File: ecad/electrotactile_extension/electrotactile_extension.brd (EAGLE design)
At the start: 80 x 38.4 mm, 376 parts, among them IC1 DRV8662, J1 VERT MALE 2.54MM, J2 VERT MALE 2.54MM, J3 VERT MALE 2.54MM, J4 VERT MALE 2.54MM, J5 VERT MALE 2.54MM, J6 PTH VERT MALE, J7 PTH VERT MALE, J8 PTH VERT MALE, J9 PTH VERT MALE, Q1 MCH3474 4A/30V, Q2 MCH3474 4A/30V, Q3 MCH3474 4A/30V, Q4 MCH3474 4A/30V, Q5 MCH3474 4A/30V, Q6 MCH3474 4A/30V, SW1 4A/28V, SW2 25mA/24V

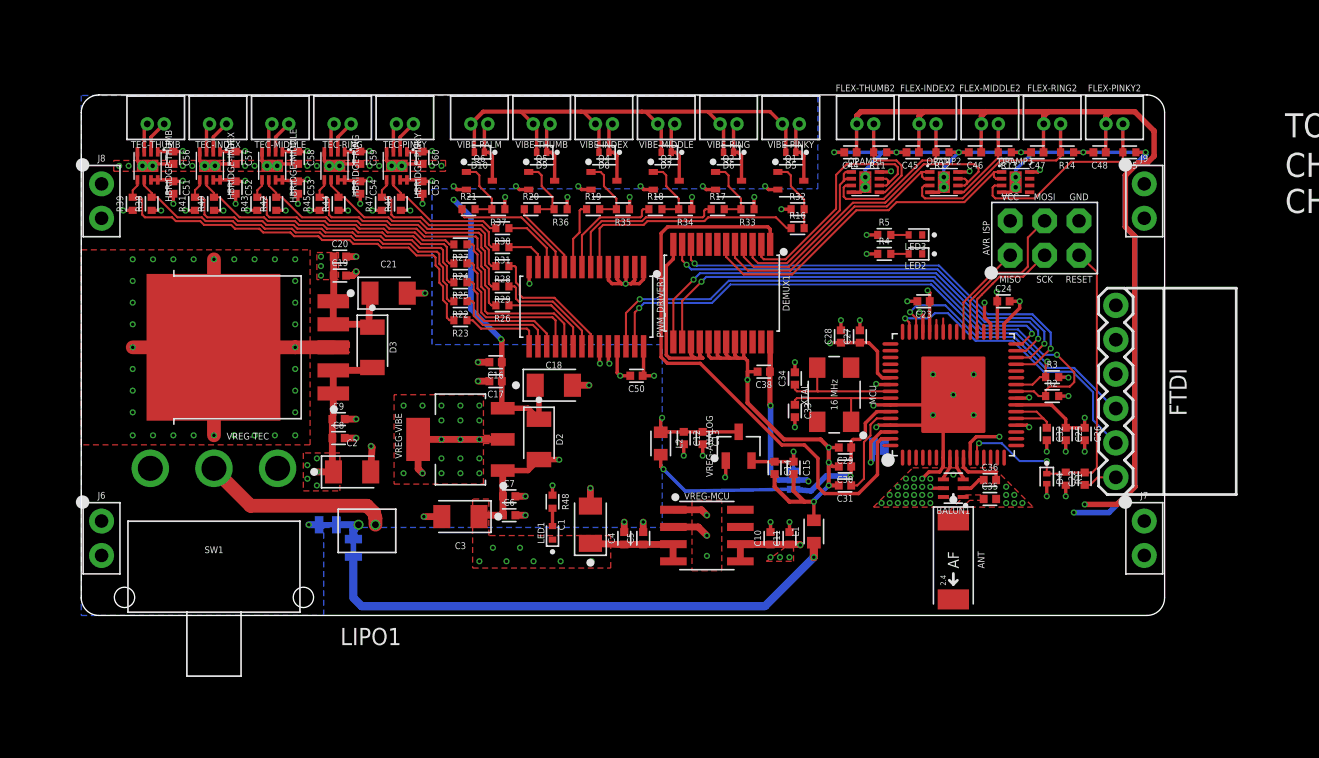
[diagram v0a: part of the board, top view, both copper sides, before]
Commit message: Create Electrotactile Extension board.
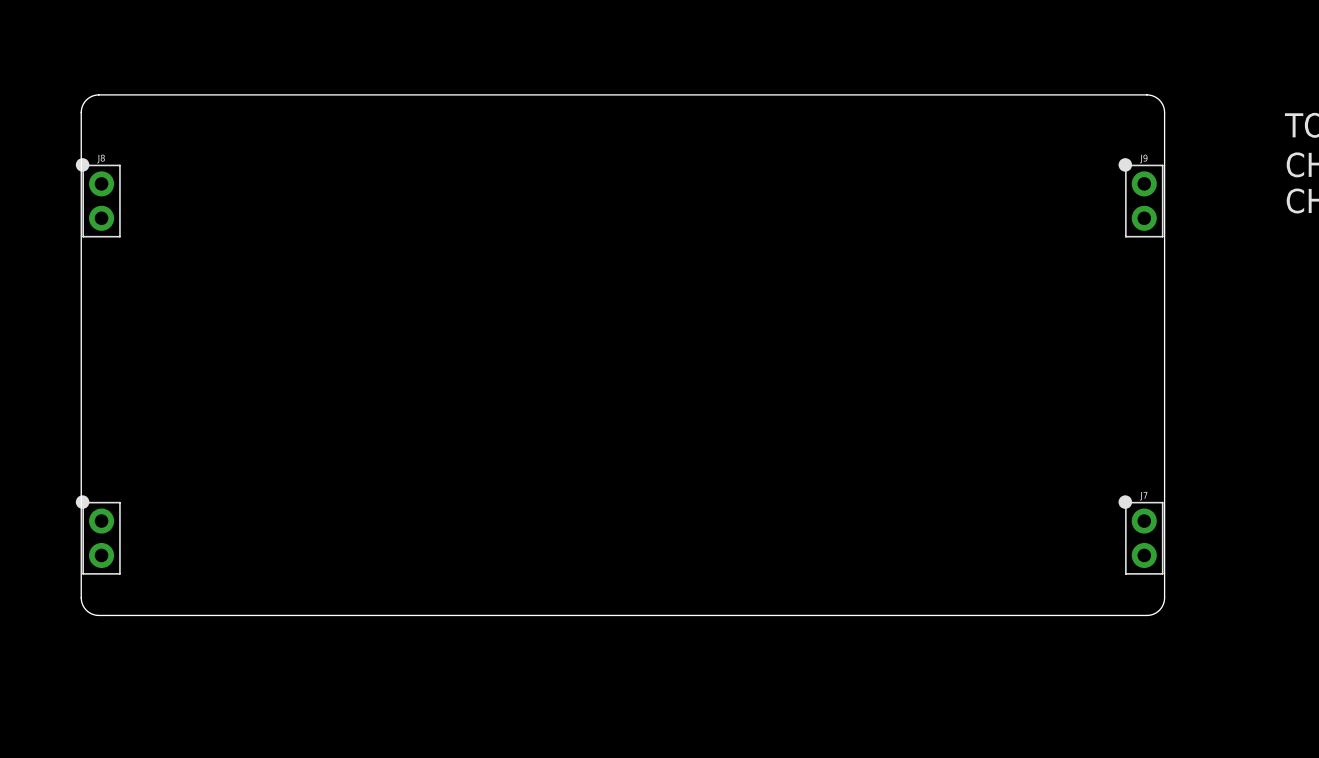
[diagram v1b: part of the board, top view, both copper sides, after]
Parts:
- removed ANT: 2.45GHz, _radio_frequency:ANTC6522X100
- removed AVR_ISP: PTH VERT MALE, _connectors:HDRV6W64P254_2X3_762X483X838B_AVR-ISP
- removed BALUN1: 50/100, _radio_frequency:RESCAXE65P200X125X95-6
- removed BR_ANALOG, BR_NOISE: NET_BRIDGE, _power_symbols:NET_BRIDGE
- removed C1, C18, C2, C21, C3: 100uF/10V, _capacitors:CAPCP3216X160
- removed C10, C13, C14, C16, C19, C22, C23, C25, C27, C30, C38, C44, C45, C46, C47, C48, C5, C50, C51, C52, C53, C54, C55, C56, C57, C58, C59, C60, C7, C9: 0.1uF/50V, _capacitors:CAPC1005X55_SMD-0402
- removed C11, C12, C15, C17, C20, C4, C6, C8: 10uF/6.3V, _capacitors:CAPC1005X55_SMD-0402
- removed C24, C26, C28, C29, C31, C32: 1uF/25V, _capacitors:CAPC1005X55_SMD-0402
- removed C33, C34: 12pF/100V, _capacitors:CAPC1005X55_SMD-0402
- removed C35: 0.75pF/50V, _capacitors:CAPC1005X55_SMD-0402
- removed C36: 22pF/100V, _capacitors:CAPC1005X55_SMD-0402
- removed D10, D4, D5, D6, D7, D8, D9: 150mA/75V, _discrete_semiconductors:DFN100X60X55-2
- removed D2, D3: 1A/50V, _discrete_semiconductors:SODFL3516X170
- removed DEMUX1: CH16_MUX-DEMUX, _special:SOP65P780X200-24
- removed FLEX-INDEX2, FLEX-MIDDLE2, FLEX-PINKY2, FLEX-RING2, FLEX-THUMB2: 10K, _sensors:_MOLEX-0530470210_VERT_PITCH-1.25MM
- removed FTDI: FTDI, _connectors:FTDI_BASIC-6PIN-MALE-RA
- removed HBRIDGE-INDEX, HBRIDGE-MIDDLE, HBRIDGE-PINKY, HBRIDGE-RING, HBRIDGE-THUMB: DRV8837C 1A, _special:WSON-8-PPAD
- removed JP1: JUMPER_SMD_3-PAD_NO_SILK, _connectors:SMT-JUMPER_3_NO_SILK
- removed JP2: JUMPER_SMD_2-PAD_NO_SILK, _connectors:SMT-JUMPER_2_NO_SILK
- removed L1, L2: 10uH/380mA, _inductors:INDC1608X60-0603
- removed LED1: BLUE, _leds:LEDC1005X40_LED-0402
- removed LED2: GREEN, _leds:LEDC1005X40_LED-0402
- removed LED3: RED, _leds:LEDC1005X40_LED-0402
- removed LIPO1: 7.4V, _batteries:BATTERY_MOLEX-0530470210_VERT_PITCH-1.25MM
- removed MCU: ATMEGA128RFA1, _ic_microcontrollers:QFN50P900X900X90-64
- removed OPAMP1, OPAMP2, OPAMP3: LM358, _op_amps:WSON-8-PPAD
- removed PWM_DRIVER1: PCA9685, _special:SOP65P650X110-28
- removed Q1, Q2, Q3, Q4, Q5, Q6: MCH3474 4A/30V, _transistors:SOTFL65P209X90-3
- removed R1, R11, R12, R13, R14, R15, R32, R33, R34, R35, R36, R37, R38, R39, R40, R41, R42, R43, R44, R45, R46, R47, R48: 10K, _resistors:RESC1005X35_SMD-0402
- removed R16, R17, R18, R19, R20, R21, R22, R23, R24, R25, R26, R27, R28, R29, R30, R31: 100, _resistors:RESC1005X35_SMD-0402
- removed R2, R3: 4.7K, _resistors:RESC1005X35_SMD-0402
- removed R4, R5: 1K, _resistors:RESC1005X35_SMD-0402
- removed SW1: 4A/28V, _switches:SW_SLIDE_SPDT_RA_PTH_12.7L-9.5W
- removed TEC-INDEX, TEC-MIDDLE, TEC-PINKY, TEC-RING, TEC-THUMB: PELTIER, _actuators:_MOLEX-0530470210_VERT_PITCH-1.25MM
- removed VIBE-INDEX, VIBE-MIDDLE, VIBE-PALM, VIBE-PINKY, VIBE-RING, VIBE-THUMB: Molex VERT 1.25mm pitch, _actuators:_MOLEX-0530470210_VERT_PITCH-1.25MM
- removed VREG-ANALOG: MCP1700-1802 1.8V/200mA, _ic_power:SOT95P237X112-3_SOT-23-3
- removed VREG-MCU: TPS76833QDR 1A/3.3V, _ic_power:SOIC127P600X265-8
- removed VREG-TEC: 3A/1.8V, _ic_power:TO170P1363X457-6
- removed VREG-VIBE: TL1963A-33 1.5A/3.3V, _ic_power:SOT229P700X180-4
- removed XTAL: 16 MHz, _crystals_oscillators_resonators:OSCCC500X320X110_CRYSTAL
- moved U$2 21.9 mm to (59.9, -8.00)
- moved U$1 20.5 mm to (44.9, -8.00)
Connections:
- removed net +: LIPO1.+, SW1.P
- removed net A1.8V: C14.1, C15.1, JP1.1, VREG-ANALOG.2
- removed net AGND: BALUN1.5, C14.2, C15.2, C29.2, C30.2, C31.2, C35.2, C36.2, C38.2, C44.2, C45.2, C46.2, C47.2, C48.2, DEMUX1.12, DEMUX1.15, DEMUX1.16, DEMUX1.17, DEMUX1.18, DEMUX1.19, DEMUX1.20, DEMUX1.21, DEMUX1.22, DEMUX1.23, DEMUX1.7, DEMUX1.8, DEMUX1.9, L1.2, MCU.10, MCU.58, MCU.61, MCU.7, MCU.EP, MCU.P$1, MCU.P$2, MCU.P$3, MCU.P$4, MCU.P$5, OPAMP1.4, OPAMP1.GND, OPAMP1.P$1, OPAMP1.P$2, OPAMP2.4, OPAMP2.GND, OPAMP2.P$1, OPAMP2.P$2, OPAMP3.4, OPAMP3.GND, OPAMP3.P$1, OPAMP3.P$2, R11.1, R12.1, R13.1, R14.1, R15.1
- removed net AREF: JP2.2, MCU.62
- removed net AVCC: C29.1, C30.1, JP1.3, L2.2, MCU.59
- removed net FLEX-INDEX2: DEMUX1.3, OPAMP1.1, OPAMP1.2
- removed net FLEX-MIDDLE2: DEMUX1.4, OPAMP2.6, OPAMP2.7
- removed net FLEX-PINKY2: DEMUX1.6, OPAMP3.1, OPAMP3.2
- removed net FLEX-RING2: DEMUX1.5, OPAMP2.1, OPAMP2.2
- removed net FLEX-THUMB2: DEMUX1.2, OPAMP1.6, OPAMP1.7
- removed net LED_RX: LED3.A, MCU.42
- removed net LED_TX: LED2.A, MCU.43
- removed net MISO: AVR_ISP.MISO, MCU.39
- removed net MOSI: AVR_ISP.MOSI, MCU.38
- removed net N$1: HBRIDGE-THUMB.3, TEC-THUMB.1
- removed net N$10: HBRIDGE-INDEX.6, R24.2, R40.2
- removed net N$10001: FLEX-PINKY2.2, OPAMP3.3, R15.2
- removed net N$1004: FLEX-THUMB2.2, OPAMP1.5, R11.2
- removed net N$11: HBRIDGE-INDEX.3, TEC-INDEX.1
- removed net N$12: HBRIDGE-MIDDLE.3, TEC-MIDDLE.1
- removed net N$13: HBRIDGE-MIDDLE.5, R27.2, R43.2
- removed net N$14: HBRIDGE-MIDDLE.6, R26.2, R42.2
- removed net N$15: D6.A, Q2.3, VIBE-RING.2
- removed net N$16: HBRIDGE-MIDDLE.2, TEC-MIDDLE.2
- removed net N$17: D5.A, Q1.3, VIBE-PINKY.2
- removed net N$18: HBRIDGE-RING.3, TEC-RING.1
- removed net N$19: HBRIDGE-RING.5, R29.2, R45.2
- removed net N$2: D8.A, Q4.3, VIBE-INDEX.2
- removed net N$20: HBRIDGE-RING.6, R28.2, R44.2
- removed net N$21: Q4.1, R19.2, R35.2
- removed net N$22: Q5.1, R20.2, R36.2
- removed net N$23: HBRIDGE-RING.2, TEC-RING.2
- removed net N$24: HBRIDGE-PINKY.3, TEC-PINKY.1
- removed net N$25: HBRIDGE-PINKY.5, R31.2, R47.2
- removed net N$26: HBRIDGE-PINKY.6, R30.2, R46.2
- removed net N$27: HBRIDGE-PINKY.2, TEC-PINKY.2
- removed net N$28: Q1.1, R16.2, R32.2
- removed net N$29: HBRIDGE-THUMB.5, R23.2, R39.2
- removed net N$3: D9.A, Q5.3, VIBE-THUMB.2
- removed net N$30: D10.A, Q6.3, VIBE-PALM.2
- removed net N$31: HBRIDGE-THUMB.6, R22.2, R38.2
- removed net N$32: Q6.1, R21.2, R37.2
- removed net N$35: C34.1, MCU.56, XTAL.3
- removed net N$36: C33.1, MCU.57, XTAL.1
- removed net N$38: FLEX-INDEX2.2, OPAMP1.3, R12.2
- removed net N$4: D7.A, Q3.3, VIBE-MIDDLE.2
- removed net N$40: BR_ANALOG.P$2, L1.1
- removed net N$41: FLEX-RING2.2, OPAMP2.3, R14.2
- removed net N$45: BALUN1.3, MCU.9
- removed net N$46: BALUN1.4, MCU.8
- removed net N$47: BALUN1.2, C36.1
- removed net N$5: HBRIDGE-THUMB.2, TEC-THUMB.2
- removed net N$50: C22.1, FTDI.DTR
- removed net N$53: LED1.K, R48.2
- removed net N$54: LED2.K, R4.2
- removed net N$55: LED3.K, R5.2
- removed net N$6: HBRIDGE-INDEX.2, TEC-INDEX.2
- removed net N$62: C32.1, MCU.21, MCU.22
- removed net N$63: C31.1, MCU.60
- removed net N$8: HBRIDGE-INDEX.5, R25.2, R41.2
- removed net N$9: Q3.1, R18.2, R34.2
- removed net N$991: FLEX-MIDDLE2.2, OPAMP2.5, R13.2
- removed net RESET: AVR_ISP.RESET, C22.2, D4.A, MCU.12, R1.1
- removed net RFSIG: ANT.1, BALUN1.1, C35.1
- removed net RX0: FTDI.TXO, MCU.46
- removed net S0: DEMUX1.10, MCU.29
- removed net S1: DEMUX1.11, MCU.30
- removed net S2: DEMUX1.14, MCU.32
- removed net S3: DEMUX1.13, MCU.31
- removed net SCK: AVR_ISP.SCK, MCU.37
- removed net SIG: DEMUX1.1, MCU.63
- removed net TEC-INDEX-COLD: PWM_DRIVER1.17, R25.1
- removed net TEC-INDEX-HOT: PWM_DRIVER1.18, R24.1
- removed net TEC-MIDDLE-COLD: PWM_DRIVER1.19, R27.1
- removed net TEC-MIDDLE-HOT: PWM_DRIVER1.20, R26.1
- removed net TEC-PINKY-COLD: PWM_DRIVER1.13, R31.1
- removed net TEC-PINKY-HOT: PWM_DRIVER1.12, R30.1
- removed net TEC-RING-COLD: PWM_DRIVER1.21, R29.1
- removed net TEC-RING-HOT: PWM_DRIVER1.22, R28.1
- removed net TEC-THUMB-COLD: PWM_DRIVER1.15, R23.1
- removed net TEC-THUMB-HOT: PWM_DRIVER1.16, R22.1
- removed net TX0: FTDI.RXI, MCU.47
- removed net VIBE-INDEX: PWM_DRIVER1.9, R19.1
- removed net VIBE-MIDDLE: PWM_DRIVER1.8, R18.1
- removed net VIBE-PALM: PWM_DRIVER1.11, R21.1
- removed net VIBE-PINKY: PWM_DRIVER1.6, R16.1
- removed net VIBE-RING: PWM_DRIVER1.7, R17.1
- removed net VIBE-THUMB: PWM_DRIVER1.10, R20.1
- removed net VSENSOR: C38.1, C44.1, C45.1, C46.1, C47.1, C48.1, DEMUX1.24, FLEX-INDEX2.1, FLEX-MIDDLE2.1, FLEX-PINKY2.1, FLEX-RING2.1, FLEX-THUMB2.1, JP1.2, JP2.1, OPAMP1.8, OPAMP2.8, OPAMP3.8
- net 1.8V: no longer C19.1, C20.1, C21.A, C56.1, C57.1, C58.1, C59.1, C60.1, D3.A, HBRIDGE-INDEX.1, HBRIDGE-MIDDLE.1, HBRIDGE-PINKY.1, HBRIDGE-RING.1, HBRIDGE-THUMB.1, VREG-TEC.4, VREG-TEC.5
- net 3.3V: no longer C16.1, C17.1, C18.A, D10.K, D2.A, D5.K, D6.K, D7.K, D8.K, D9.K, VIBE-INDEX.1, VIBE-MIDDLE.1, VIBE-PALM.1, VIBE-PINKY.1, VIBE-RING.1, VIBE-THUMB.1, VREG-VIBE.3
- net GND: now also J6.2; no longer AVR_ISP.GND, BR_ANALOG.P$1, BR_NOISE.P$2, C10.2, C11.2, C12.2, C13.2, C23.2, C24.2, C25.2, C26.2, C27.2, C28.2, C32.2, C33.2, C34.2, C50.2, C51.2, C52.2, C53.2, C54.2, C55.2, FTDI.GND, LIPO1.-, MCU.11, MCU.20, MCU.24, MCU.33, MCU.35, MCU.45, MCU.55, PWM_DRIVER1.1, PWM_DRIVER1.14, PWM_DRIVER1.2, PWM_DRIVER1.23, PWM_DRIVER1.24, PWM_DRIVER1.25, PWM_DRIVER1.3, PWM_DRIVER1.4, PWM_DRIVER1.5, R32.1, R33.1, R34.1, R35.1, R36.1, R37.1, R38.1, R39.1, R4.1, R40.1, R41.1, R42.1, R43.1, R44.1, R45.1, R46.1, R47.1, R5.1, VREG-ANALOG.1, VREG-MCU.1, VREG-MCU.2
- net N$7: no longer Q2.1, R17.2, R33.2
- net NGND: no longer BR_NOISE.P$1, C1.K, C16.2, C17.2, C18.K, C19.2, C2.K, C20.2, C21.K, C3.K, C4.2, C5.2, C56.2, C57.2, C58.2, C59.2, C6.2, C60.2, C7.2, C8.2, C9.2, HBRIDGE-INDEX.4, HBRIDGE-INDEX.GND, HBRIDGE-INDEX.P$1, HBRIDGE-INDEX.P$2, HBRIDGE-MIDDLE.4, HBRIDGE-MIDDLE.GND, HBRIDGE-MIDDLE.P$1, HBRIDGE-MIDDLE.P$2, HBRIDGE-PINKY.4, HBRIDGE-PINKY.GND, HBRIDGE-PINKY.P$1, HBRIDGE-PINKY.P$2, HBRIDGE-RING.4, HBRIDGE-RING.GND, HBRIDGE-RING.P$1, HBRIDGE-RING.P$2, HBRIDGE-THUMB.4, HBRIDGE-THUMB.GND, HBRIDGE-THUMB.P$1, HBRIDGE-THUMB.P$2, Q1.2, Q2.2, Q3.2, Q4.2, Q5.2, Q6.2, R48.1, VREG-TEC.3, VREG-TEC.TAB, VREG-VIBE.2, VREG-VIBE.TAB
- net SCL: now also J7.2; no longer MCU.25, PWM_DRIVER1.26, R2.1
- net SDA: now also J7.1; no longer MCU.26, PWM_DRIVER1.27, R3.1
- net VBAT: now also J6.1; no longer C1.A, C2.A, C3.A, C4.1, C5.1, C6.1, C7.1, C8.1, C9.1, D2.K, D3.K, LED1.A, SW1.S1, VREG-MCU.3, VREG-MCU.4, VREG-TEC.1, VREG-TEC.2, VREG-VIBE.1
- net VCC: no longer C10.1, C11.1, C12.1, C13.1, C23.1, C24.1, C25.1, C26.1, C27.1, C28.1, C50.1, C51.1, C52.1, C53.1, C54.1, C55.1, D4.K, HBRIDGE-INDEX.7, HBRIDGE-INDEX.8, HBRIDGE-MIDDLE.7, HBRIDGE-MIDDLE.8, HBRIDGE-PINKY.7, HBRIDGE-PINKY.8, HBRIDGE-RING.7, HBRIDGE-RING.8, HBRIDGE-THUMB.7, HBRIDGE-THUMB.8, L2.1, MCU.23, MCU.34, MCU.44, MCU.54, PWM_DRIVER1.28, R1.2, R2.2, R3.2, VREG-ANALOG.3, VREG-MCU.5, VREG-MCU.6
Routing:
- net AGND: track 187.8 -> 0.00 mm, vias 43 -> 0
- net VSENSOR: track 138.6 -> 0.00 mm, vias 7 -> 0
- net NGND: track 75.4 -> 0.00 mm, vias 86 -> 0
- net 3.3V: track 71.4 -> 0.00 mm, vias 2 -> 0
- net GND: track 65.9 -> 0.00 mm, vias 51 -> 0
- net VCC: track 50.3 -> 0.00 mm, vias 19 -> 0
- net SCL: track 45.2 -> 0.00 mm, vias 2 -> 0
- net SIG: track 44.0 -> 0.00 mm
- net N$40: track 39.9 -> 0.00 mm, vias 1 -> 0
- net SDA: track 39.8 -> 0.00 mm, vias 2 -> 0
- net S3: track 35.2 -> 0.00 mm, vias 2 -> 0
- net S0: track 34.1 -> 0.00 mm, vias 2 -> 0
- net S1: track 33.5 -> 0.00 mm, vias 2 -> 0
- net S2: track 32.9 -> 0.00 mm, vias 2 -> 0
- net N$29: track 31.7 -> 0.00 mm
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- removed copper zone on layer 1, net 1.8V
- removed copper zone on layer 2, net 1.8V
- removed copper zone on layer 1, net AGND
- removed copper zone on layer 15, net AGND
- removed copper zone on layer 1, net GND
- removed copper zone on layer 15, net N$34
- removed copper zone on layer 2, net N$34
- removed copper zone on layer 2, net N$37
- removed copper zone on layer 1, net NGND
- removed copper zone on layer 15, net NGND
- removed copper zone on layer 16, net NGND
- removed copper zone on layer 1, net RFSIG
- removed copper zone on layer 1, net VBAT
- removed copper zone on layer 2, net VBAT
- removed copper zone on layer 1, net VCC
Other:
- board text removed: "Designed by: &"

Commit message: Update work on Electrotactile extension board.  Add doc folder with several schematics breaking down the transmission of touch for documentation purposes.
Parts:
- removed ET_INDEX_PIXEL1-10, ET_INDEX_PIXEL1-11, ET_INDEX_PIXEL1-12, ET_INDEX_PIXEL1-13, ET_INDEX_PIXEL1-14, ET_INDEX_PIXEL1-15, ET_INDEX_PIXEL1-16, ET_INDEX_PIXEL1-17, ET_INDEX_PIXEL1-18, ET_INDEX_PIXEL1-19, ET_INDEX_PIXEL1-20, ET_INDEX_PIXEL1-5, ET_INDEX_PIXEL1-6, ET_INDEX_PIXEL1-7, ET_INDEX_PIXEL1-8, ET_INDEX_PIXEL1-9, ET_INDEX_PIXEL2-10, ET_INDEX_PIXEL2-11, ET_INDEX_PIXEL2-12, ET_INDEX_PIXEL2-13, ET_INDEX_PIXEL2-14, ET_INDEX_PIXEL2-15, ET_INDEX_PIXEL2-16, ET_INDEX_PIXEL2-17, ET_INDEX_PIXEL2-18, ET_INDEX_PIXEL2-19, ET_INDEX_PIXEL2-20, ET_INDEX_PIXEL2-5, ET_INDEX_PIXEL2-6, ET_INDEX_PIXEL2-7, ET_INDEX_PIXEL2-8, ET_INDEX_PIXEL2-9, ET_INDEX_PIXEL3-10, ET_INDEX_PIXEL3-11, ET_INDEX_PIXEL3-12, ET_INDEX_PIXEL3-13, ET_INDEX_PIXEL3-14, ET_INDEX_PIXEL3-15, ET_INDEX_PIXEL3-16, ET_INDEX_PIXEL3-17, ET_INDEX_PIXEL3-18, ET_INDEX_PIXEL3-19, ET_INDEX_PIXEL3-20, ET_INDEX_PIXEL3-5, ET_INDEX_PIXEL3-6, ET_INDEX_PIXEL3-7, ET_INDEX_PIXEL3-8, ET_INDEX_PIXEL3-9, ET_INDEX_PIXEL4-10, ET_INDEX_PIXEL4-11, ET_INDEX_PIXEL4-12, ET_INDEX_PIXEL4-13, ET_INDEX_PIXEL4-14, ET_INDEX_PIXEL4-15, ET_INDEX_PIXEL4-16, ET_INDEX_PIXEL4-17, ET_INDEX_PIXEL4-18, ET_INDEX_PIXEL4-19, ET_INDEX_PIXEL4-20, ET_INDEX_PIXEL4-5, ET_INDEX_PIXEL4-6, ET_INDEX_PIXEL4-7, ET_INDEX_PIXEL4-8, ET_INDEX_PIXEL4-9: SPST-NO 170mA 250V, _relay:SOP254P609X203-4
- removed PWM_DRIVER2, PWM_DRIVER3, PWM_DRIVER4, PWM_DRIVER5, PWM_DRIVER6: PCA9685, _special:SOP65P650X110-28
- added ET_MIDDLE_PIXEL1-1, ET_MIDDLE_PIXEL1-2, ET_MIDDLE_PIXEL1-3, ET_MIDDLE_PIXEL1-4, ET_MIDDLE_PIXEL2-1, ET_MIDDLE_PIXEL2-2, ET_MIDDLE_PIXEL2-3, ET_MIDDLE_PIXEL2-4, ET_MIDDLE_PIXEL3-1, ET_MIDDLE_PIXEL3-2, ET_MIDDLE_PIXEL3-3, ET_MIDDLE_PIXEL3-4, ET_MIDDLE_PIXEL4-1, ET_MIDDLE_PIXEL4-2, ET_MIDDLE_PIXEL4-3, ET_MIDDLE_PIXEL4-4, ET_PINKY_PIXEL1-1, ET_PINKY_PIXEL1-2, ET_PINKY_PIXEL1-3, ET_PINKY_PIXEL1-4, ET_PINKY_PIXEL2-1, ET_PINKY_PIXEL2-2, ET_PINKY_PIXEL2-3, ET_PINKY_PIXEL2-4, ET_PINKY_PIXEL3-1, ET_PINKY_PIXEL3-2, ET_PINKY_PIXEL3-3, ET_PINKY_PIXEL3-4, ET_PINKY_PIXEL4-1, ET_PINKY_PIXEL4-2, ET_PINKY_PIXEL4-3, ET_PINKY_PIXEL4-4, ET_RING_PIXEL1-1, ET_RING_PIXEL1-2, ET_RING_PIXEL1-3, ET_RING_PIXEL1-4, ET_RING_PIXEL2-1, ET_RING_PIXEL2-2, ET_RING_PIXEL2-3, ET_RING_PIXEL2-4, ET_RING_PIXEL3-1, ET_RING_PIXEL3-2, ET_RING_PIXEL3-3, ET_RING_PIXEL3-4, ET_RING_PIXEL4-1, ET_RING_PIXEL4-2, ET_RING_PIXEL4-3, ET_RING_PIXEL4-4, ET_THUMB_PIXEL1-1, ET_THUMB_PIXEL1-2, ET_THUMB_PIXEL1-3, ET_THUMB_PIXEL1-4, ET_THUMB_PIXEL2-1, ET_THUMB_PIXEL2-2, ET_THUMB_PIXEL2-3, ET_THUMB_PIXEL2-4, ET_THUMB_PIXEL3-1, ET_THUMB_PIXEL3-2, ET_THUMB_PIXEL3-3, ET_THUMB_PIXEL3-4, ET_THUMB_PIXEL4-1, ET_THUMB_PIXEL4-2, ET_THUMB_PIXEL4-3, ET_THUMB_PIXEL4-4: SPST-NO 170mA 250V, _relay:SOP254P609X203-4
- added MUX_INDEX, MUX_MIDDLE, MUX_PINKY, MUX_RING, MUX_THUMB: PCA9685, _special:SOP65P650X110-28
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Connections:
- new net MIDDLE_IN1-1: ET_MIDDLE_PIXEL1-1.1, MUX_MIDDLE.21
- new net MIDDLE_IN1-2: ET_MIDDLE_PIXEL1-2.1, MUX_MIDDLE.19
- new net MIDDLE_IN1-3: ET_MIDDLE_PIXEL1-3.1, MUX_MIDDLE.17
- new net MIDDLE_IN1-4: ET_MIDDLE_PIXEL1-4.1, MUX_MIDDLE.15
- new net MIDDLE_IN2-1: ET_MIDDLE_PIXEL2-1.1, MUX_MIDDLE.22
- new net MIDDLE_IN2-2: ET_MIDDLE_PIXEL2-2.1, MUX_MIDDLE.20
- new net MIDDLE_IN2-3: ET_MIDDLE_PIXEL2-3.1, MUX_MIDDLE.18
- new net MIDDLE_IN2-4: ET_MIDDLE_PIXEL2-4.1, MUX_MIDDLE.16
- new net MIDDLE_IN3-1: ET_MIDDLE_PIXEL3-1.1, MUX_MIDDLE.12
- new net MIDDLE_IN3-2: ET_MIDDLE_PIXEL3-2.1, MUX_MIDDLE.10
- new net MIDDLE_IN3-3: ET_MIDDLE_PIXEL3-3.1, MUX_MIDDLE.8
- new net MIDDLE_IN3-4: ET_MIDDLE_PIXEL3-4.1, MUX_MIDDLE.6
- new net MIDDLE_IN4-1: ET_MIDDLE_PIXEL4-1.1, MUX_MIDDLE.13
- new net MIDDLE_IN4-2: ET_MIDDLE_PIXEL4-2.1, MUX_MIDDLE.11
- new net MIDDLE_IN4-3: ET_MIDDLE_PIXEL4-3.1, MUX_MIDDLE.9
- new net MIDDLE_IN4-4: ET_MIDDLE_PIXEL4-4.1, MUX_MIDDLE.7
- new net MIDDLE_OUT1-1: ET_MIDDLE_PIXEL1-1.3
- new net MIDDLE_OUT1-2: ET_MIDDLE_PIXEL1-2.3
- new net MIDDLE_OUT1-3: ET_MIDDLE_PIXEL1-3.3
- new net MIDDLE_OUT1-4: ET_MIDDLE_PIXEL1-4.3
- new net MIDDLE_OUT2-1: ET_MIDDLE_PIXEL2-1.3
- new net MIDDLE_OUT2-2: ET_MIDDLE_PIXEL2-2.3
- new net MIDDLE_OUT2-3: ET_MIDDLE_PIXEL2-3.3
- new net MIDDLE_OUT2-4: ET_MIDDLE_PIXEL2-4.3
- new net MIDDLE_OUT3-1: ET_MIDDLE_PIXEL3-1.3
- new net MIDDLE_OUT3-2: ET_MIDDLE_PIXEL3-2.3
- new net MIDDLE_OUT3-3: ET_MIDDLE_PIXEL3-3.3
- new net MIDDLE_OUT3-4: ET_MIDDLE_PIXEL3-4.3
- new net MIDDLE_OUT4-1: ET_MIDDLE_PIXEL4-1.3
- new net MIDDLE_OUT4-2: ET_MIDDLE_PIXEL4-2.3
- new net MIDDLE_OUT4-3: ET_MIDDLE_PIXEL4-3.3
- new net MIDDLE_OUT4-4: ET_MIDDLE_PIXEL4-4.3
- new net PINKY_IN1-1: ET_PINKY_PIXEL1-1.1, MUX_PINKY.22
- new net PINKY_IN1-2: ET_PINKY_PIXEL1-2.1, MUX_PINKY.20
- new net PINKY_IN1-3: ET_PINKY_PIXEL1-3.1, MUX_PINKY.18
- new net PINKY_IN1-4: ET_PINKY_PIXEL1-4.1, MUX_PINKY.16
- new net PINKY_IN2-1: ET_PINKY_PIXEL2-1.1, MUX_PINKY.21
- new net PINKY_IN2-2: ET_PINKY_PIXEL2-2.1, MUX_PINKY.19
- new net PINKY_IN2-3: ET_PINKY_PIXEL2-3.1, MUX_PINKY.17
- new net PINKY_IN2-4: ET_PINKY_PIXEL2-4.1, MUX_PINKY.15
- new net PINKY_IN3-1: ET_PINKY_PIXEL3-1.1, MUX_PINKY.13
- new net PINKY_IN3-2: ET_PINKY_PIXEL3-2.1, MUX_PINKY.11
- new net PINKY_IN3-3: ET_PINKY_PIXEL3-3.1, MUX_PINKY.9
- new net PINKY_IN3-4: ET_PINKY_PIXEL3-4.1, MUX_PINKY.7
- new net PINKY_IN4-1: ET_PINKY_PIXEL4-1.1, MUX_PINKY.12
- new net PINKY_IN4-2: ET_PINKY_PIXEL4-2.1, MUX_PINKY.10
- new net PINKY_IN4-3: ET_PINKY_PIXEL4-3.1, MUX_PINKY.8
- new net PINKY_IN4-4: ET_PINKY_PIXEL4-4.1, MUX_PINKY.6
- new net PINKY_OUT1-1: ET_PINKY_PIXEL1-1.3
- new net PINKY_OUT1-2: ET_PINKY_PIXEL1-2.3
- new net PINKY_OUT1-3: ET_PINKY_PIXEL1-3.3
- new net PINKY_OUT1-4: ET_PINKY_PIXEL1-4.3
- new net PINKY_OUT2-1: ET_PINKY_PIXEL2-1.3
- new net PINKY_OUT2-2: ET_PINKY_PIXEL2-2.3
- new net PINKY_OUT2-3: ET_PINKY_PIXEL2-3.3
- new net PINKY_OUT2-4: ET_PINKY_PIXEL2-4.3
- new net PINKY_OUT3-1: ET_PINKY_PIXEL3-1.3
- new net PINKY_OUT3-2: ET_PINKY_PIXEL3-2.3
- new net PINKY_OUT3-3: ET_PINKY_PIXEL3-3.3
- new net PINKY_OUT3-4: ET_PINKY_PIXEL3-4.3
- new net PINKY_OUT4-1: ET_PINKY_PIXEL4-1.3
- new net PINKY_OUT4-2: ET_PINKY_PIXEL4-2.3
- new net PINKY_OUT4-3: ET_PINKY_PIXEL4-3.3
- new net PINKY_OUT4-4: ET_PINKY_PIXEL4-4.3
- new net RING_IN1-1: ET_RING_PIXEL1-1.1, MUX_RING.7
- new net RING_IN1-2: ET_RING_PIXEL1-2.1, MUX_RING.9
- new net RING_IN1-3: ET_RING_PIXEL1-3.1, MUX_RING.11
- new net RING_IN1-4: ET_RING_PIXEL1-4.1, MUX_RING.13
- new net RING_IN2-1: ET_RING_PIXEL2-1.1, MUX_RING.6
- new net RING_IN2-2: ET_RING_PIXEL2-2.1, MUX_RING.8
- new net RING_IN2-3: ET_RING_PIXEL2-3.1, MUX_RING.10
- new net RING_IN2-4: ET_RING_PIXEL2-4.1, MUX_RING.12
- new net RING_IN3-1: ET_RING_PIXEL3-1.1, MUX_RING.16
- new net RING_IN3-2: ET_RING_PIXEL3-2.1, MUX_RING.18
- new net RING_IN3-3: ET_RING_PIXEL3-3.1, MUX_RING.20
- new net RING_IN3-4: ET_RING_PIXEL3-4.1, MUX_RING.22
- new net RING_IN4-1: ET_RING_PIXEL4-1.1, MUX_RING.15
- new net RING_IN4-2: ET_RING_PIXEL4-2.1, MUX_RING.17
- new net RING_IN4-3: ET_RING_PIXEL4-3.1, MUX_RING.19
- new net RING_IN4-4: ET_RING_PIXEL4-4.1, MUX_RING.21
- new net RING_OUT1-1: ET_RING_PIXEL1-1.3
- new net RING_OUT1-2: ET_RING_PIXEL1-2.3
- new net RING_OUT1-3: ET_RING_PIXEL1-3.3
- new net RING_OUT1-4: ET_RING_PIXEL1-4.3
- new net RING_OUT2-1: ET_RING_PIXEL2-1.3
- new net RING_OUT2-2: ET_RING_PIXEL2-2.3
- new net RING_OUT2-3: ET_RING_PIXEL2-3.3
- new net RING_OUT2-4: ET_RING_PIXEL2-4.3
- new net RING_OUT3-1: ET_RING_PIXEL3-1.3
- new net RING_OUT3-2: ET_RING_PIXEL3-2.3
- new net RING_OUT3-3: ET_RING_PIXEL3-3.3
- new net RING_OUT3-4: ET_RING_PIXEL3-4.3
- new net RING_OUT4-1: ET_RING_PIXEL4-1.3
- new net RING_OUT4-2: ET_RING_PIXEL4-2.3
- new net RING_OUT4-3: ET_RING_PIXEL4-3.3
- new net RING_OUT4-4: ET_RING_PIXEL4-4.3
- new net THUMB_IN1-1: ET_THUMB_PIXEL1-1.1, MUX_THUMB.6
- new net THUMB_IN1-2: ET_THUMB_PIXEL1-2.1, MUX_THUMB.7
- new net THUMB_IN1-3: ET_THUMB_PIXEL1-3.1, MUX_THUMB.8
- new net THUMB_IN1-4: ET_THUMB_PIXEL1-4.1, MUX_THUMB.9
- new net THUMB_IN2-1: ET_THUMB_PIXEL2-1.1, MUX_THUMB.10
- new net THUMB_IN2-2: ET_THUMB_PIXEL2-2.1, MUX_THUMB.11
- new net THUMB_IN2-3: ET_THUMB_PIXEL2-3.1, MUX_THUMB.12
- new net THUMB_IN2-4: ET_THUMB_PIXEL2-4.1, MUX_THUMB.13
- new net THUMB_IN3-1: ET_THUMB_PIXEL3-1.1, MUX_THUMB.15
- new net THUMB_IN3-2: ET_THUMB_PIXEL3-2.1, MUX_THUMB.16
- new net THUMB_IN3-3: ET_THUMB_PIXEL3-3.1, MUX_THUMB.17
- new net THUMB_IN3-4: ET_THUMB_PIXEL3-4.1, MUX_THUMB.18
- new net THUMB_IN4-1: ET_THUMB_PIXEL4-1.1, MUX_THUMB.19
- new net THUMB_IN4-2: ET_THUMB_PIXEL4-2.1, MUX_THUMB.20
- new net THUMB_IN4-3: ET_THUMB_PIXEL4-3.1, MUX_THUMB.21
- new net THUMB_IN4-4: ET_THUMB_PIXEL4-4.1, MUX_THUMB.22
- new net THUMB_OUT1-1: ET_THUMB_PIXEL1-1.3
- new net THUMB_OUT1-2: ET_THUMB_PIXEL1-2.3
- new net THUMB_OUT1-3: ET_THUMB_PIXEL1-3.3
- new net THUMB_OUT1-4: ET_THUMB_PIXEL1-4.3
- new net THUMB_OUT2-1: ET_THUMB_PIXEL2-1.3
- new net THUMB_OUT2-2: ET_THUMB_PIXEL2-2.3
- new net THUMB_OUT2-3: ET_THUMB_PIXEL2-3.3
- new net THUMB_OUT2-4: ET_THUMB_PIXEL2-4.3
- new net THUMB_OUT3-1: ET_THUMB_PIXEL3-1.3
- new net THUMB_OUT3-2: ET_THUMB_PIXEL3-2.3
- new net THUMB_OUT3-3: ET_THUMB_PIXEL3-3.3
- new net THUMB_OUT3-4: ET_THUMB_PIXEL3-4.3
- new net THUMB_OUT4-1: ET_THUMB_PIXEL4-1.3
- new net THUMB_OUT4-2: ET_THUMB_PIXEL4-2.3
- new net THUMB_OUT4-3: ET_THUMB_PIXEL4-3.3
- new net THUMB_OUT4-4: ET_THUMB_PIXEL4-4.3
- net GND: now also MUX_INDEX.1, MUX_INDEX.14, MUX_INDEX.2, MUX_INDEX.23, MUX_INDEX.24, MUX_INDEX.25, MUX_INDEX.3, MUX_INDEX.4, MUX_INDEX.5, MUX_MIDDLE.1, MUX_MIDDLE.14, MUX_MIDDLE.2, MUX_MIDDLE.23, MUX_MIDDLE.24, MUX_MIDDLE.25, MUX_MIDDLE.3, MUX_MIDDLE.4, MUX_MIDDLE.5, MUX_PINKY.1, MUX_PINKY.14, MUX_PINKY.2, MUX_PINKY.23, MUX_PINKY.24, MUX_PINKY.25, MUX_PINKY.3, MUX_PINKY.4, MUX_PINKY.5, MUX_RING.1, MUX_RING.14, MUX_RING.2, MUX_RING.23, MUX_RING.24, MUX_RING.25, MUX_RING.3, MUX_RING.4, MUX_RING.5, MUX_THUMB.1, MUX_THUMB.14, MUX_THUMB.2, MUX_THUMB.23, MUX_THUMB.24, MUX_THUMB.25, MUX_THUMB.3, MUX_THUMB.4, MUX_THUMB.5; no longer PWM_DRIVER2.1, PWM_DRIVER2.14, PWM_DRIVER2.2, PWM_DRIVER2.23, PWM_DRIVER2.24, PWM_DRIVER2.25, PWM_DRIVER2.3, PWM_DRIVER2.4, PWM_DRIVER2.5, PWM_DRIVER3.1, PWM_DRIVER3.14, PWM_DRIVER3.2, PWM_DRIVER3.23, PWM_DRIVER3.24, PWM_DRIVER3.25, PWM_DRIVER3.3, PWM_DRIVER3.4, PWM_DRIVER3.5, PWM_DRIVER4.1, PWM_DRIVER4.14, PWM_DRIVER4.2, PWM_DRIVER4.23, PWM_DRIVER4.24, PWM_DRIVER4.25, PWM_DRIVER4.3, PWM_DRIVER4.4, PWM_DRIVER4.5, PWM_DRIVER5.1, PWM_DRIVER5.14, PWM_DRIVER5.2, PWM_DRIVER5.23, PWM_DRIVER5.24, PWM_DRIVER5.25, PWM_DRIVER5.3, PWM_DRIVER5.4, PWM_DRIVER5.5, PWM_DRIVER6.1, PWM_DRIVER6.14, PWM_DRIVER6.2, PWM_DRIVER6.23, PWM_DRIVER6.24, PWM_DRIVER6.25, PWM_DRIVER6.3, PWM_DRIVER6.4, PWM_DRIVER6.5
- net INDEX_IN1-1: now also MUX_INDEX.6; no longer ET_INDEX_PIXEL1-13.1, ET_INDEX_PIXEL1-17.1, ET_INDEX_PIXEL1-5.1, ET_INDEX_PIXEL1-9.1, PWM_DRIVER2.6, PWM_DRIVER3.6, PWM_DRIVER4.6, PWM_DRIVER5.6, PWM_DRIVER6.6
- net INDEX_IN1-2: now also MUX_INDEX.8; no longer ET_INDEX_PIXEL1-10.1, ET_INDEX_PIXEL1-14.1, ET_INDEX_PIXEL1-18.1, ET_INDEX_PIXEL1-6.1, PWM_DRIVER2.7, PWM_DRIVER3.7, PWM_DRIVER4.7, PWM_DRIVER5.7, PWM_DRIVER6.7
- net INDEX_IN1-3: now also MUX_INDEX.10; no longer ET_INDEX_PIXEL1-11.1, ET_INDEX_PIXEL1-15.1, ET_INDEX_PIXEL1-19.1, ET_INDEX_PIXEL1-7.1, PWM_DRIVER2.8, PWM_DRIVER3.8, PWM_DRIVER4.8, PWM_DRIVER5.8, PWM_DRIVER6.8
- net INDEX_IN1-4: now also MUX_INDEX.12; no longer ET_INDEX_PIXEL1-12.1, ET_INDEX_PIXEL1-16.1, ET_INDEX_PIXEL1-20.1, ET_INDEX_PIXEL1-8.1, PWM_DRIVER2.9, PWM_DRIVER3.9, PWM_DRIVER4.9, PWM_DRIVER5.9, PWM_DRIVER6.9
- net INDEX_IN2-1: now also MUX_INDEX.7; no longer ET_INDEX_PIXEL2-11.1, ET_INDEX_PIXEL2-15.1, ET_INDEX_PIXEL2-19.1, ET_INDEX_PIXEL2-7.1, PWM_DRIVER2.10, PWM_DRIVER3.10, PWM_DRIVER4.10, PWM_DRIVER5.10, PWM_DRIVER6.10
- net INDEX_IN2-2: now also MUX_INDEX.9; no longer ET_INDEX_PIXEL2-10.1, ET_INDEX_PIXEL2-14.1, ET_INDEX_PIXEL2-18.1, ET_INDEX_PIXEL2-6.1, PWM_DRIVER2.11, PWM_DRIVER3.11, PWM_DRIVER4.11, PWM_DRIVER5.11, PWM_DRIVER6.11
- net INDEX_IN2-3: now also MUX_INDEX.11; no longer ET_INDEX_PIXEL2-13.1, ET_INDEX_PIXEL2-17.1, ET_INDEX_PIXEL2-5.1, ET_INDEX_PIXEL2-9.1, PWM_DRIVER2.12, PWM_DRIVER3.12, PWM_DRIVER4.12, PWM_DRIVER5.12, PWM_DRIVER6.12
- net INDEX_IN2-4: now also MUX_INDEX.13; no longer ET_INDEX_PIXEL2-12.1, ET_INDEX_PIXEL2-16.1, ET_INDEX_PIXEL2-20.1, ET_INDEX_PIXEL2-8.1, PWM_DRIVER2.13, PWM_DRIVER3.13, PWM_DRIVER4.13, PWM_DRIVER5.13, PWM_DRIVER6.13
- net INDEX_IN3-1: now also MUX_INDEX.15; no longer ET_INDEX_PIXEL3-13.1, ET_INDEX_PIXEL3-17.1, ET_INDEX_PIXEL3-5.1, ET_INDEX_PIXEL3-9.1, PWM_DRIVER2.15, PWM_DRIVER3.15, PWM_DRIVER4.15, PWM_DRIVER5.15, PWM_DRIVER6.15
- net INDEX_IN3-2: now also MUX_INDEX.17; no longer ET_INDEX_PIXEL3-10.1, ET_INDEX_PIXEL3-14.1, ET_INDEX_PIXEL3-18.1, ET_INDEX_PIXEL3-6.1, PWM_DRIVER2.16, PWM_DRIVER3.16, PWM_DRIVER4.16, PWM_DRIVER5.16, PWM_DRIVER6.16
- net INDEX_IN3-3: now also MUX_INDEX.19; no longer ET_INDEX_PIXEL3-11.1, ET_INDEX_PIXEL3-15.1, ET_INDEX_PIXEL3-19.1, ET_INDEX_PIXEL3-7.1, PWM_DRIVER2.17, PWM_DRIVER3.17, PWM_DRIVER4.17, PWM_DRIVER5.17, PWM_DRIVER6.17
- net INDEX_IN3-4: now also MUX_INDEX.21; no longer ET_INDEX_PIXEL3-12.1, ET_INDEX_PIXEL3-16.1, ET_INDEX_PIXEL3-20.1, ET_INDEX_PIXEL3-8.1, PWM_DRIVER2.18, PWM_DRIVER3.18, PWM_DRIVER4.18, PWM_DRIVER5.18, PWM_DRIVER6.18
- net INDEX_IN4-1: now also MUX_INDEX.16; no longer ET_INDEX_PIXEL4-13.1, ET_INDEX_PIXEL4-17.1, ET_INDEX_PIXEL4-5.1, ET_INDEX_PIXEL4-9.1, PWM_DRIVER2.19, PWM_DRIVER3.19, PWM_DRIVER4.19, PWM_DRIVER5.19, PWM_DRIVER6.19
- net INDEX_IN4-2: now also MUX_INDEX.18; no longer ET_INDEX_PIXEL4-10.1, ET_INDEX_PIXEL4-14.1, ET_INDEX_PIXEL4-18.1, ET_INDEX_PIXEL4-6.1, PWM_DRIVER2.20, PWM_DRIVER3.20, PWM_DRIVER4.20, PWM_DRIVER5.20, PWM_DRIVER6.20
- net INDEX_IN4-3: now also MUX_INDEX.20; no longer ET_INDEX_PIXEL4-11.1, ET_INDEX_PIXEL4-15.1, ET_INDEX_PIXEL4-19.1, ET_INDEX_PIXEL4-7.1, PWM_DRIVER2.21, PWM_DRIVER3.21, PWM_DRIVER4.21, PWM_DRIVER5.21, PWM_DRIVER6.21
- net INDEX_IN4-4: now also MUX_INDEX.22; no longer ET_INDEX_PIXEL4-12.1, ET_INDEX_PIXEL4-16.1, ET_INDEX_PIXEL4-20.1, ET_INDEX_PIXEL4-8.1, PWM_DRIVER2.22, PWM_DRIVER3.22, PWM_DRIVER4.22, PWM_DRIVER5.22, PWM_DRIVER6.22
- net INDEX_OUT1-1: no longer ET_INDEX_PIXEL1-13.3, ET_INDEX_PIXEL1-17.3, ET_INDEX_PIXEL1-5.3, ET_INDEX_PIXEL1-9.3
- net INDEX_OUT1-2: no longer ET_INDEX_PIXEL1-10.3, ET_INDEX_PIXEL1-14.3, ET_INDEX_PIXEL1-18.3, ET_INDEX_PIXEL1-6.3
- net INDEX_OUT1-3: no longer ET_INDEX_PIXEL1-11.3, ET_INDEX_PIXEL1-15.3, ET_INDEX_PIXEL1-19.3, ET_INDEX_PIXEL1-7.3
- net INDEX_OUT1-4: no longer ET_INDEX_PIXEL1-12.3, ET_INDEX_PIXEL1-16.3, ET_INDEX_PIXEL1-20.3, ET_INDEX_PIXEL1-8.3
- net INDEX_OUT2-1: no longer ET_INDEX_PIXEL2-11.3, ET_INDEX_PIXEL2-15.3, ET_INDEX_PIXEL2-19.3, ET_INDEX_PIXEL2-7.3
- net INDEX_OUT2-2: no longer ET_INDEX_PIXEL2-10.3, ET_INDEX_PIXEL2-14.3, ET_INDEX_PIXEL2-18.3, ET_INDEX_PIXEL2-6.3
- net INDEX_OUT2-3: no longer ET_INDEX_PIXEL2-13.3, ET_INDEX_PIXEL2-17.3, ET_INDEX_PIXEL2-5.3, ET_INDEX_PIXEL2-9.3
- net INDEX_OUT2-4: no longer ET_INDEX_PIXEL2-12.3, ET_INDEX_PIXEL2-16.3, ET_INDEX_PIXEL2-20.3, ET_INDEX_PIXEL2-8.3
- net INDEX_OUT3-1: no longer ET_INDEX_PIXEL3-13.3, ET_INDEX_PIXEL3-17.3, ET_INDEX_PIXEL3-5.3, ET_INDEX_PIXEL3-9.3
- net INDEX_OUT3-2: no longer ET_INDEX_PIXEL3-10.3, ET_INDEX_PIXEL3-14.3, ET_INDEX_PIXEL3-18.3, ET_INDEX_PIXEL3-6.3
- net INDEX_OUT3-3: no longer ET_INDEX_PIXEL3-11.3, ET_INDEX_PIXEL3-15.3, ET_INDEX_PIXEL3-19.3, ET_INDEX_PIXEL3-7.3
- net INDEX_OUT3-4: no longer ET_INDEX_PIXEL3-12.3, ET_INDEX_PIXEL3-16.3, ET_INDEX_PIXEL3-20.3, ET_INDEX_PIXEL3-8.3
- net INDEX_OUT4-1: no longer ET_INDEX_PIXEL4-13.3, ET_INDEX_PIXEL4-17.3, ET_INDEX_PIXEL4-5.3, ET_INDEX_PIXEL4-9.3
- net INDEX_OUT4-2: no longer ET_INDEX_PIXEL4-10.3, ET_INDEX_PIXEL4-14.3, ET_INDEX_PIXEL4-18.3, ET_INDEX_PIXEL4-6.3
- net INDEX_OUT4-3: no longer ET_INDEX_PIXEL4-11.3, ET_INDEX_PIXEL4-15.3, ET_INDEX_PIXEL4-19.3, ET_INDEX_PIXEL4-7.3
- net INDEX_OUT4-4: no longer ET_INDEX_PIXEL4-12.3, ET_INDEX_PIXEL4-16.3, ET_INDEX_PIXEL4-20.3, ET_INDEX_PIXEL4-8.3
- net N$100: now also ET_MIDDLE_PIXEL3-4.2; no longer ET_INDEX_PIXEL3-12.2
- net N$101: now also ET_MIDDLE_PIXEL4-1.2; no longer ET_INDEX_PIXEL4-9.2
- net N$102: now also ET_MIDDLE_PIXEL4-2.2; no longer ET_INDEX_PIXEL4-10.2
- net N$103: now also ET_MIDDLE_PIXEL4-3.2; no longer ET_INDEX_PIXEL4-11.2
- net N$104: now also ET_MIDDLE_PIXEL4-4.2; no longer ET_INDEX_PIXEL4-12.2
- net N$105: now also ET_RING_PIXEL1-1.2; no longer ET_INDEX_PIXEL1-13.2
- net N$106: now also ET_RING_PIXEL1-2.2; no longer ET_INDEX_PIXEL1-14.2
- net N$107: now also ET_RING_PIXEL1-3.2; no longer ET_INDEX_PIXEL1-15.2
- net N$108: now also ET_RING_PIXEL1-4.2; no longer ET_INDEX_PIXEL1-16.2
- net N$109: now also ET_RING_PIXEL2-1.2; no longer ET_INDEX_PIXEL2-15.2
- net N$110: now also ET_RING_PIXEL2-2.2; no longer ET_INDEX_PIXEL2-14.2
- net N$111: now also ET_RING_PIXEL2-3.2; no longer ET_INDEX_PIXEL2-13.2
- net N$112: now also ET_RING_PIXEL2-4.2; no longer ET_INDEX_PIXEL2-16.2
- net N$113: now also ET_RING_PIXEL3-1.2; no longer ET_INDEX_PIXEL3-13.2
- net N$114: now also ET_RING_PIXEL3-2.2; no longer ET_INDEX_PIXEL3-14.2
- net N$115: now also ET_RING_PIXEL3-3.2; no longer ET_INDEX_PIXEL3-15.2
- net N$116: now also ET_RING_PIXEL3-4.2; no longer ET_INDEX_PIXEL3-16.2
- net N$117: now also ET_RING_PIXEL4-1.2; no longer ET_INDEX_PIXEL4-13.2
- net N$118: now also ET_RING_PIXEL4-2.2; no longer ET_INDEX_PIXEL4-14.2
- net N$119: now also ET_RING_PIXEL4-3.2; no longer ET_INDEX_PIXEL4-15.2
- net N$120: now also ET_RING_PIXEL4-4.2; no longer ET_INDEX_PIXEL4-16.2
- net N$121: now also ET_PINKY_PIXEL1-1.2; no longer ET_INDEX_PIXEL1-17.2
- net N$122: now also ET_PINKY_PIXEL1-2.2; no longer ET_INDEX_PIXEL1-18.2
- net N$123: now also ET_PINKY_PIXEL1-3.2; no longer ET_INDEX_PIXEL1-19.2
- net N$124: now also ET_PINKY_PIXEL1-4.2; no longer ET_INDEX_PIXEL1-20.2
- net N$125: now also ET_PINKY_PIXEL2-1.2; no longer ET_INDEX_PIXEL2-19.2
- net N$126: now also ET_PINKY_PIXEL2-2.2; no longer ET_INDEX_PIXEL2-18.2
- net N$127: now also ET_PINKY_PIXEL2-3.2; no longer ET_INDEX_PIXEL2-17.2
- net N$128: now also ET_PINKY_PIXEL2-4.2; no longer ET_INDEX_PIXEL2-20.2
- net N$129: now also ET_PINKY_PIXEL3-1.2; no longer ET_INDEX_PIXEL3-17.2
- net N$130: now also ET_PINKY_PIXEL3-2.2; no longer ET_INDEX_PIXEL3-18.2
- net N$131: now also ET_PINKY_PIXEL3-3.2; no longer ET_INDEX_PIXEL3-19.2
- net N$132: now also ET_PINKY_PIXEL3-4.2; no longer ET_INDEX_PIXEL3-20.2
- net N$133: now also ET_PINKY_PIXEL4-1.2; no longer ET_INDEX_PIXEL4-17.2
- net N$134: now also ET_PINKY_PIXEL4-2.2; no longer ET_INDEX_PIXEL4-18.2
- net N$135: now also ET_PINKY_PIXEL4-3.2; no longer ET_INDEX_PIXEL4-19.2
- net N$136: now also ET_PINKY_PIXEL4-4.2; no longer ET_INDEX_PIXEL4-20.2
- net N$58: now also ET_THUMB_PIXEL1-1.2; no longer ET_INDEX_PIXEL1-5.2
- net N$74: now also ET_THUMB_PIXEL1-2.2; no longer ET_INDEX_PIXEL1-6.2
- net N$75: now also ET_THUMB_PIXEL1-3.2; no longer ET_INDEX_PIXEL1-7.2
- net N$76: now also ET_THUMB_PIXEL1-4.2; no longer ET_INDEX_PIXEL1-8.2
- net N$77: now also ET_THUMB_PIXEL2-1.2; no longer ET_INDEX_PIXEL2-7.2
- net N$78: now also ET_THUMB_PIXEL2-2.2; no longer ET_INDEX_PIXEL2-6.2
- net N$79: now also ET_THUMB_PIXEL2-3.2; no longer ET_INDEX_PIXEL2-5.2
- net N$80: now also ET_THUMB_PIXEL2-4.2; no longer ET_INDEX_PIXEL2-8.2
- net N$81: now also ET_THUMB_PIXEL3-1.2; no longer ET_INDEX_PIXEL3-5.2
- net N$82: now also ET_THUMB_PIXEL3-2.2; no longer ET_INDEX_PIXEL3-6.2
- net N$83: now also ET_THUMB_PIXEL3-3.2; no longer ET_INDEX_PIXEL3-7.2
- net N$84: now also ET_THUMB_PIXEL3-4.2; no longer ET_INDEX_PIXEL3-8.2
- net N$85: now also ET_THUMB_PIXEL4-1.2; no longer ET_INDEX_PIXEL4-5.2
- net N$86: now also ET_THUMB_PIXEL4-2.2; no longer ET_INDEX_PIXEL4-6.2
- net N$87: now also ET_THUMB_PIXEL4-3.2; no longer ET_INDEX_PIXEL4-7.2
- net N$88: now also ET_THUMB_PIXEL4-4.2; no longer ET_INDEX_PIXEL4-8.2
- net N$89: now also ET_MIDDLE_PIXEL1-1.2; no longer ET_INDEX_PIXEL1-9.2
- net N$90: now also ET_MIDDLE_PIXEL1-2.2; no longer ET_INDEX_PIXEL1-10.2
- net N$91: now also ET_MIDDLE_PIXEL1-3.2; no longer ET_INDEX_PIXEL1-11.2
- net N$92: now also ET_MIDDLE_PIXEL1-4.2; no longer ET_INDEX_PIXEL1-12.2
- net N$93: now also ET_MIDDLE_PIXEL2-1.2; no longer ET_INDEX_PIXEL2-11.2
- net N$94: now also ET_MIDDLE_PIXEL2-2.2; no longer ET_INDEX_PIXEL2-10.2
- net N$95: now also ET_MIDDLE_PIXEL2-3.2; no longer ET_INDEX_PIXEL2-9.2
- net N$96: now also ET_MIDDLE_PIXEL2-4.2; no longer ET_INDEX_PIXEL2-12.2
- net N$97: now also ET_MIDDLE_PIXEL3-1.2; no longer ET_INDEX_PIXEL3-9.2
- net N$98: now also ET_MIDDLE_PIXEL3-2.2; no longer ET_INDEX_PIXEL3-10.2
- net N$99: now also ET_MIDDLE_PIXEL3-3.2; no longer ET_INDEX_PIXEL3-11.2
- net SCL: now also MUX_INDEX.26, MUX_MIDDLE.26, MUX_PINKY.26, MUX_RING.26, MUX_THUMB.26; no longer PWM_DRIVER2.26, PWM_DRIVER3.26, PWM_DRIVER4.26, PWM_DRIVER5.26, PWM_DRIVER6.26
- net SDA: now also MUX_INDEX.27, MUX_MIDDLE.27, MUX_PINKY.27, MUX_RING.27, MUX_THUMB.27; no longer PWM_DRIVER2.27, PWM_DRIVER3.27, PWM_DRIVER4.27, PWM_DRIVER5.27, PWM_DRIVER6.27
- net V+: now also ET_MIDDLE_PIXEL1-1.4, ET_MIDDLE_PIXEL1-2.4, ET_MIDDLE_PIXEL1-3.4, ET_MIDDLE_PIXEL1-4.4, ET_MIDDLE_PIXEL2-1.4, ET_MIDDLE_PIXEL2-2.4, ET_MIDDLE_PIXEL2-3.4, ET_MIDDLE_PIXEL2-4.4, ET_MIDDLE_PIXEL3-1.4, ET_MIDDLE_PIXEL3-2.4, ET_MIDDLE_PIXEL3-3.4, ET_MIDDLE_PIXEL3-4.4, ET_MIDDLE_PIXEL4-1.4, ET_MIDDLE_PIXEL4-2.4, ET_MIDDLE_PIXEL4-3.4, ET_MIDDLE_PIXEL4-4.4, ET_PINKY_PIXEL1-1.4, ET_PINKY_PIXEL1-2.4, ET_PINKY_PIXEL1-3.4, ET_PINKY_PIXEL1-4.4, ET_PINKY_PIXEL2-1.4, ET_PINKY_PIXEL2-2.4, ET_PINKY_PIXEL2-3.4, ET_PINKY_PIXEL2-4.4, ET_PINKY_PIXEL3-1.4, ET_PINKY_PIXEL3-2.4, ET_PINKY_PIXEL3-3.4, ET_PINKY_PIXEL3-4.4, ET_PINKY_PIXEL4-1.4, ET_PINKY_PIXEL4-2.4, ET_PINKY_PIXEL4-3.4, ET_PINKY_PIXEL4-4.4, ET_RING_PIXEL1-1.4, ET_RING_PIXEL1-2.4, ET_RING_PIXEL1-3.4, ET_RING_PIXEL1-4.4, ET_RING_PIXEL2-1.4, ET_RING_PIXEL2-2.4, ET_RING_PIXEL2-3.4, ET_RING_PIXEL2-4.4, ET_RING_PIXEL3-1.4, ET_RING_PIXEL3-2.4, ET_RING_PIXEL3-3.4, ET_RING_PIXEL3-4.4, ET_RING_PIXEL4-1.4, ET_RING_PIXEL4-2.4, ET_RING_PIXEL4-3.4, ET_RING_PIXEL4-4.4, ET_THUMB_PIXEL1-1.4, ET_THUMB_PIXEL1-2.4, ET_THUMB_PIXEL1-3.4, ET_THUMB_PIXEL1-4.4, ET_THUMB_PIXEL2-1.4, ET_THUMB_PIXEL2-2.4, ET_THUMB_PIXEL2-3.4, ET_THUMB_PIXEL2-4.4, ET_THUMB_PIXEL3-1.4, ET_THUMB_PIXEL3-2.4, ET_THUMB_PIXEL3-3.4, ET_THUMB_PIXEL3-4.4, ET_THUMB_PIXEL4-1.4, ET_THUMB_PIXEL4-2.4, ET_THUMB_PIXEL4-3.4, ET_THUMB_PIXEL4-4.4; no longer ET_INDEX_PIXEL1-10.4, ET_INDEX_PIXEL1-11.4, ET_INDEX_PIXEL1-12.4, ET_INDEX_PIXEL1-13.4, ET_INDEX_PIXEL1-14.4, ET_INDEX_PIXEL1-15.4, ET_INDEX_PIXEL1-16.4, ET_INDEX_PIXEL1-17.4, ET_INDEX_PIXEL1-18.4, ET_INDEX_PIXEL1-19.4, ET_INDEX_PIXEL1-20.4, ET_INDEX_PIXEL1-5.4, ET_INDEX_PIXEL1-6.4, ET_INDEX_PIXEL1-7.4, ET_INDEX_PIXEL1-8.4, ET_INDEX_PIXEL1-9.4, ET_INDEX_PIXEL2-10.4, ET_INDEX_PIXEL2-11.4, ET_INDEX_PIXEL2-12.4, ET_INDEX_PIXEL2-13.4, ET_INDEX_PIXEL2-14.4, ET_INDEX_PIXEL2-15.4, ET_INDEX_PIXEL2-16.4, ET_INDEX_PIXEL2-17.4, ET_INDEX_PIXEL2-18.4, ET_INDEX_PIXEL2-19.4, ET_INDEX_PIXEL2-20.4, ET_INDEX_PIXEL2-5.4, ET_INDEX_PIXEL2-6.4, ET_INDEX_PIXEL2-7.4, ET_INDEX_PIXEL2-8.4, ET_INDEX_PIXEL2-9.4, ET_INDEX_PIXEL3-10.4, ET_INDEX_PIXEL3-11.4, ET_INDEX_PIXEL3-12.4, ET_INDEX_PIXEL3-13.4, ET_INDEX_PIXEL3-14.4, ET_INDEX_PIXEL3-15.4, ET_INDEX_PIXEL3-16.4, ET_INDEX_PIXEL3-17.4, ET_INDEX_PIXEL3-18.4, ET_INDEX_PIXEL3-19.4, ET_INDEX_PIXEL3-20.4, ET_INDEX_PIXEL3-5.4, ET_INDEX_PIXEL3-6.4, ET_INDEX_PIXEL3-7.4, ET_INDEX_PIXEL3-8.4, ET_INDEX_PIXEL3-9.4, ET_INDEX_PIXEL4-10.4, ET_INDEX_PIXEL4-11.4, ET_INDEX_PIXEL4-12.4, ET_INDEX_PIXEL4-13.4, ET_INDEX_PIXEL4-14.4, ET_INDEX_PIXEL4-15.4, ET_INDEX_PIXEL4-16.4, ET_INDEX_PIXEL4-17.4, ET_INDEX_PIXEL4-18.4, ET_INDEX_PIXEL4-19.4, ET_INDEX_PIXEL4-20.4, ET_INDEX_PIXEL4-5.4, ET_INDEX_PIXEL4-6.4, ET_INDEX_PIXEL4-7.4, ET_INDEX_PIXEL4-8.4, ET_INDEX_PIXEL4-9.4
- net VCC: now also MUX_INDEX.28, MUX_MIDDLE.28, MUX_PINKY.28, MUX_RING.28, MUX_THUMB.28; no longer PWM_DRIVER2.28, PWM_DRIVER3.28, PWM_DRIVER4.28, PWM_DRIVER5.28, PWM_DRIVER6.28
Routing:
- net MIDDLE_IN3-4: track 0.00 -> 32.6 mm
- net RING_IN3-4: track 0.00 -> 32.1 mm
- net PINKY_IN1-1: track 0.00 -> 31.7 mm
- net INDEX_IN1-1: track 0.00 -> 30.5 mm
- net MIDDLE_IN1-1: track 0.00 -> 30.1 mm
- net RING_IN1-1: track 0.00 -> 29.9 mm
- net PINKY_IN3-4: track 0.00 -> 29.6 mm
- net PINKY_IN1-2: track 0.00 -> 29.1 mm
- net INDEX_IN3-4: track 0.00 -> 28.9 mm
- net MIDDLE_IN1-4: track 0.00 -> 28.4 mm
- net RING_IN1-4: track 0.00 -> 28.0 mm
- net INDEX_IN1-2: track 0.00 -> 27.6 mm
- net MIDDLE_IN1-2: track 0.00 -> 27.0 mm
- net RING_IN1-2: track 0.00 -> 26.8 mm
- net MIDDLE_IN3-3: track 0.00 -> 26.6 mm
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- added copper zone on layer 1, net GND
- added copper zone on layer 16, net GND
- removed copper zone on layer 15, net GND
- removed copper zone on layer 2, net VCC
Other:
- board text added: "Electrotactile Extension Rev 3"
- board text removed: "CHECK new pins used (Demux) CHECK RESISTOR VALUE FOR NEW FLEX SENSORS"
- board text removed: "TODO"
- board text removed: "Touch Glove Rev 3"
